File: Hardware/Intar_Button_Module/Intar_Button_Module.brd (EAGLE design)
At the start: 17.8 x 25.9 mm, 19 parts, among them J1 GROVE-4P-2.0-3470130P1, Q1 MMBT2222A, Q2 MMBT2222A

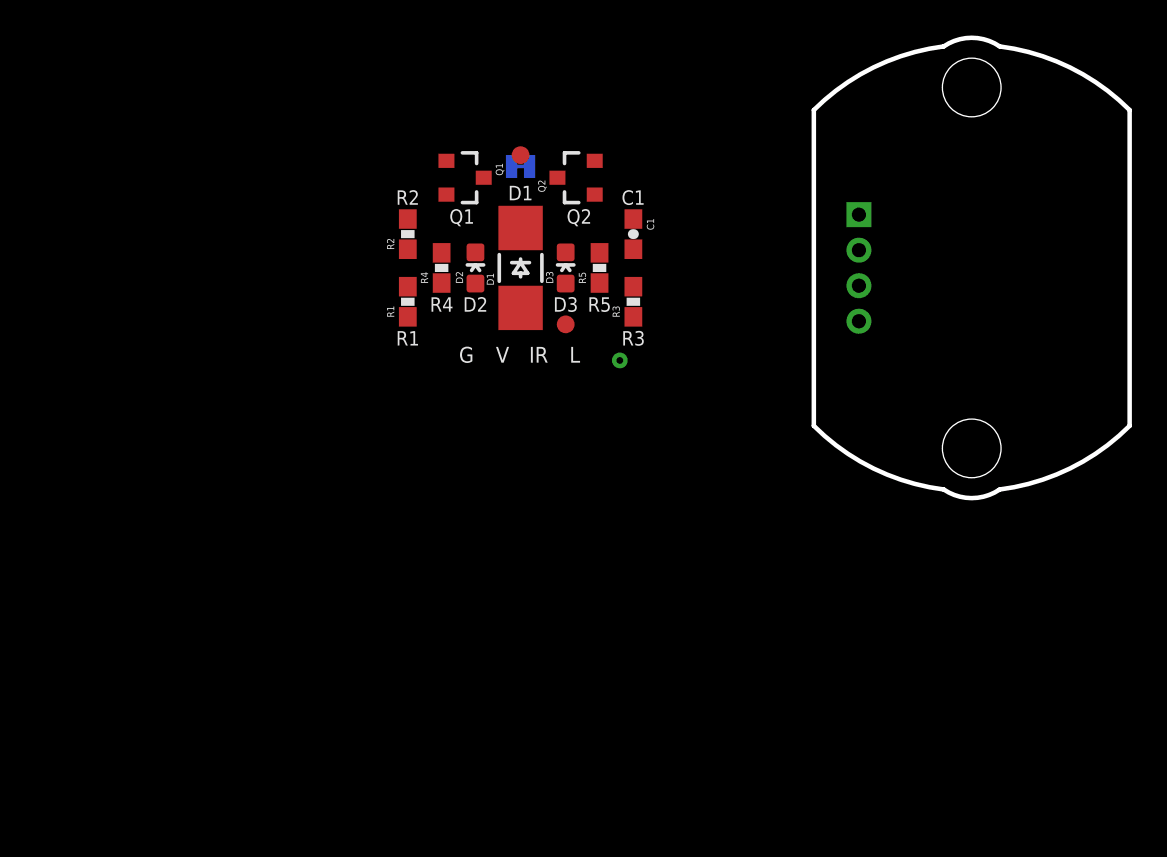
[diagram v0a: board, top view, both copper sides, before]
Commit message: Created LP5521 part
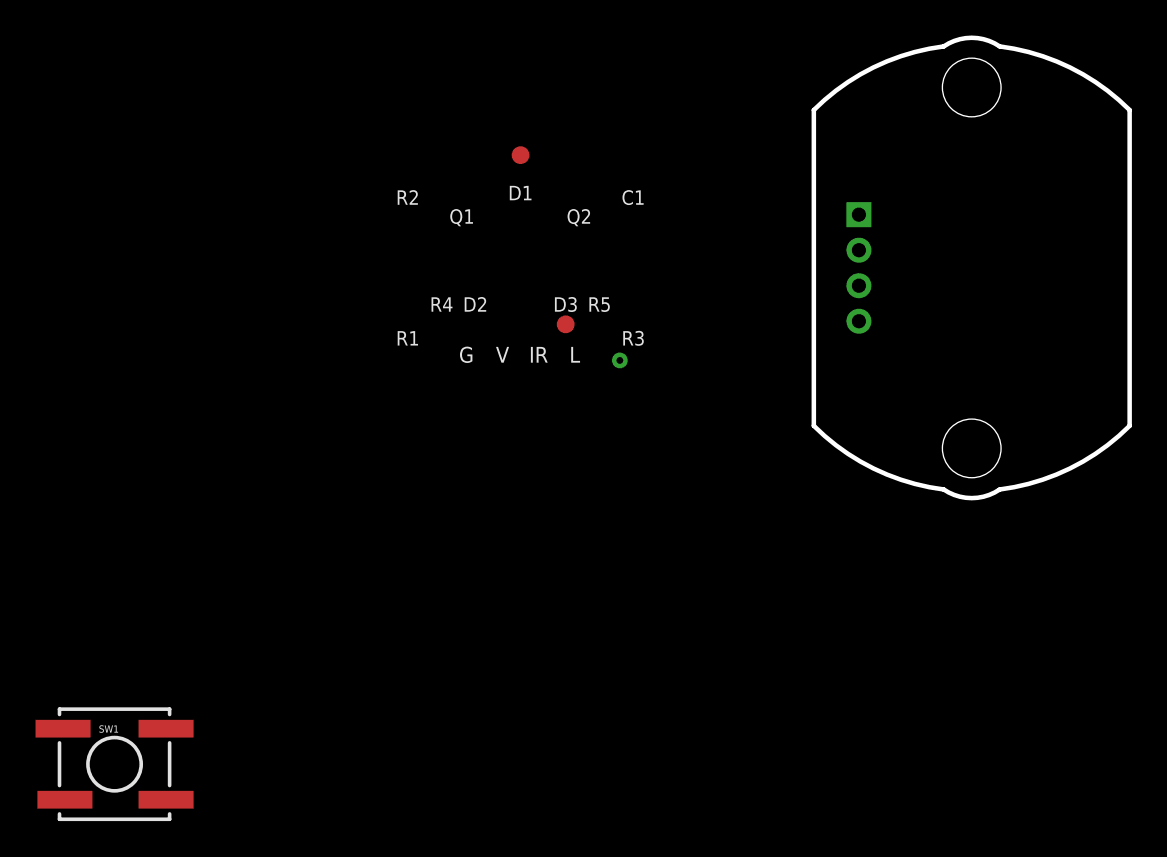
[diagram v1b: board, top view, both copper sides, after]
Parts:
- removed C1: DNP, SparkFun-Capacitors:0603-CAP
- removed D1: IR, Intar_Eagle_Library:IR42-21C/TR8
- removed D2, D3: (no value), SparkFun-LED:LED-0603
- removed Q1, Q2: MMBT2222A, SparkFun-DiscreteSemi:SOT23-3
- removed R1: 33, SparkFun-Resistors:0603-RES
- removed R2, R3: 2.2k, SparkFun-Resistors:0603-RES
- removed R4, R5: *, SparkFun-Resistors:0603-RES
- removed SJ1: JUMPER-PAD-2-NC_BY_TRACE, SparkFun-Passives:PAD-JUMPER-2-NC_BY_TRACE_YES_SILK
- added SW1: SWITCH_MOMENTARY, Intar_Eagle_Library:KSCXXXG
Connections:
- removed net IR: J1.2, R2.1
- removed net LEDS: J1.1, R3.1
- removed net N$1: Q1.1, R2.2
- removed net N$2: D1.A, R1.1
- removed net N$3: C1.1, D1.C, Q1.3
- removed net N$4: D2.C, D3.C, SJ1.2
- removed net N$5: Q2.1, R3.2
- removed net N$6: D2.A, R4.1
- removed net N$7: D3.A, R5.1
- removed net N$8: Q2.3, SJ1.1
- new net BUTTON: J1.1
- net GND: no longer C1.2, Q1.2, Q2.2
- net VCC: no longer R1.2, R4.2, R5.2
